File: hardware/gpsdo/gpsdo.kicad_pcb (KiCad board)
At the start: 2 copper layers, 6 parts, among them U1 74HC4040D_652, U2 74HC4040D_652

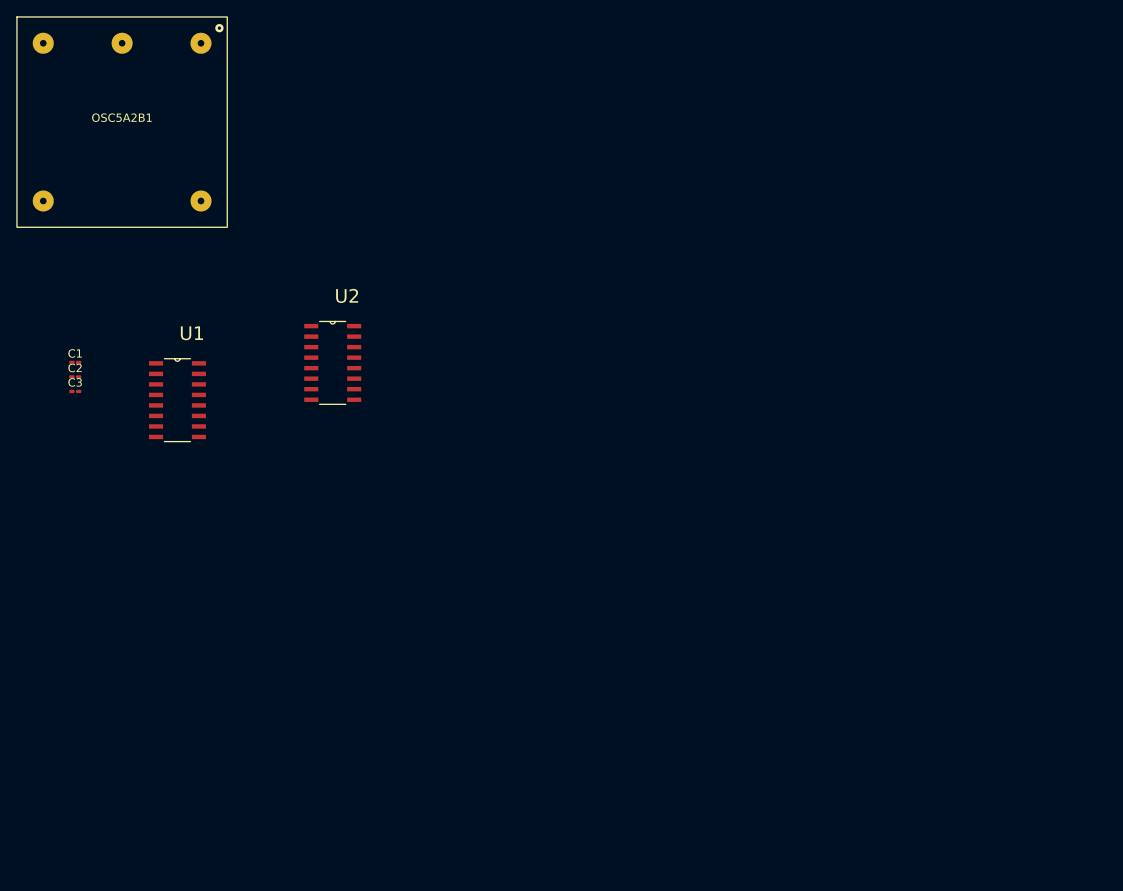
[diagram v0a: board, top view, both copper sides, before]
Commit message: update pcb; update hal
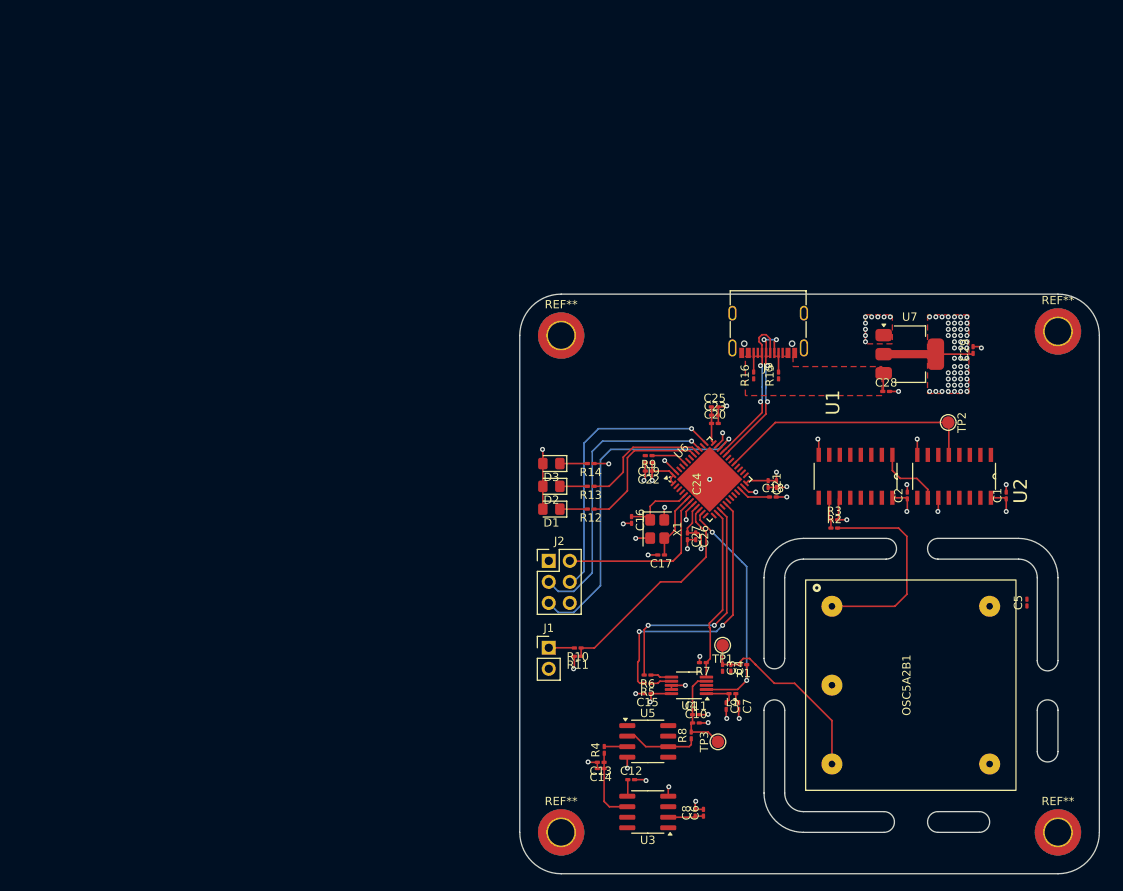
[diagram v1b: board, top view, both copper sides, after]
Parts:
- added C10: 10u, Capacitor_SMD:C_0201_0603Metric_Pad0.64x0.40mm_HandSolder, F.Cu at (129.0, 116.5)
- added C11: 100n, Capacitor_SMD:C_0201_0603Metric_Pad0.64x0.40mm_HandSolder, F.Cu at (129.0, 115.5)
- added C12: 1u, Capacitor_SMD:C_0201_0603Metric_Pad0.64x0.40mm_HandSolder, F.Cu at (121.2, 123.4)
- added C13: 10u, Capacitor_SMD:C_0201_0603Metric_Pad0.64x0.40mm_HandSolder, F.Cu at (117.5, 121.3)
- added C14: 100n, Capacitor_SMD:C_0201_0603Metric_Pad0.64x0.40mm_HandSolder, F.Cu at (117.5, 122.0)
- added C15: 100n, Capacitor_SMD:C_0201_0603Metric_Pad0.64x0.40mm_HandSolder, F.Cu at (123.2, 113.0)
- added C16: 12p, Capacitor_SMD:C_0201_0603Metric_Pad0.64x0.40mm_HandSolder, F.Cu at (121.2, 92.0)
- added C17: 12p, Capacitor_SMD:C_0201_0603Metric_Pad0.64x0.40mm_HandSolder, F.Cu at (124.8, 96.2)
- added C18: 4.7u, Capacitor_SMD:C_0201_0603Metric_Pad0.64x0.40mm_HandSolder, F.Cu at (138.3, 89.2)
- added C19: 100n, Capacitor_SMD:C_0201_0603Metric_Pad0.64x0.40mm_HandSolder, F.Cu at (123.3, 85.1)
- added C20: 100n, Capacitor_SMD:C_0201_0603Metric_Pad0.64x0.40mm_HandSolder, F.Cu at (131.3, 80.4)
- added C21: 100n, Capacitor_SMD:C_0201_0603Metric_Pad0.64x0.40mm_HandSolder, F.Cu at (137.8, 87.7)
- added C22: 100n, Capacitor_SMD:C_0201_0603Metric_Pad0.64x0.40mm_HandSolder, F.Cu at (123.3, 86.1)
- added C23: 100n, Capacitor_SMD:C_0201_0603Metric_Pad0.64x0.40mm_HandSolder, F.Cu at (131.3, 79.4)
- added C24: 100n, Capacitor_SMD:C_0201_0603Metric_Pad0.64x0.40mm_HandSolder, F.Cu at (138.8, 87.7)
- added C25: 4.7u, Capacitor_SMD:C_0201_0603Metric_Pad0.64x0.40mm_HandSolder, F.Cu at (131.3, 78.4)
- added C26: 1u, Capacitor_SMD:C_0201_0603Metric_Pad0.64x0.40mm_HandSolder, F.Cu at (129.0, 94.0)
- added C27: 100n, Capacitor_SMD:C_0201_0603Metric_Pad0.64x0.40mm_HandSolder, F.Cu at (128.0, 94.0)
- added C28: 10u, Capacitor_SMD:C_0201_0603Metric_Pad0.64x0.40mm_HandSolder, F.Cu at (152.0, 76.5)
- added C29: 10u, Capacitor_SMD:C_0201_0603Metric_Pad0.64x0.40mm_HandSolder, F.Cu at (162.5, 71.5)
- added C4: 100n, Capacitor_SMD:C_0201_0603Metric_Pad0.64x0.40mm_HandSolder, F.Cu at (133.2, 109.9)
- added C5: 100n, Capacitor_SMD:C_0201_0603Metric_Pad0.64x0.40mm_HandSolder, F.Cu at (169.0, 102.0)
- added C6: 1u, Capacitor_SMD:C_0201_0603Metric_Pad0.64x0.40mm_HandSolder, F.Cu at (129.9, 127.4)
- added C7: 100n, Capacitor_SMD:C_0201_0603Metric_Pad0.64x0.40mm_HandSolder, F.Cu at (134.2, 114.5)
- added C8: 100n, Capacitor_SMD:C_0201_0603Metric_Pad0.64x0.40mm_HandSolder, F.Cu at (128.9, 127.4)
- added C9: 100n, Capacitor_SMD:C_0201_0603Metric_Pad0.64x0.40mm_HandSolder, F.Cu at (132.7, 114.5)
- added D1: LED, LED_SMD:LED_0805_2012Metric_Pad1.15x1.40mm_HandSolder, F.Cu at (111.6, 90.7)
- added D2: LED, LED_SMD:LED_0805_2012Metric_Pad1.15x1.40mm_HandSolder, F.Cu at (111.6, 88.0)
- added D3: LED, LED_SMD:LED_0805_2012Metric_Pad1.15x1.40mm_HandSolder, F.Cu at (111.6, 85.2)
- added J1: Conn_01x02, Connector_PinHeader_2.54mm:PinHeader_1x02_P2.54mm_Vertical, F.Cu at (111.2, 107.5)
- added J2: Conn_02x03_Top_Bottom, Connector_PinHeader_2.54mm:PinHeader_2x03_P2.54mm_Vertical, F.Cu at (111.2, 97.0)
- added J3: USB_C_Receptacle_USB2.0_14P, Connector_USB:USB_C_Receptacle_G-Switch_GT-USB-7010ASV, F.Cu at (137.8, 68.1)
- added L1: 10u, Capacitor_SMD:C_0201_0603Metric_Pad0.64x0.40mm_HandSolder, F.Cu at (133.4, 113.0)
- added R1: 100, Resistor_SMD:R_0201_0603Metric_Pad0.64x0.40mm_HandSolder, F.Cu at (134.8, 109.5)
- added R10: 1.1k, Resistor_SMD:R_0201_0603Metric_Pad0.64x0.40mm_HandSolder, F.Cu at (114.8, 107.5)
- added R11: 2.2k, Resistor_SMD:R_0201_0603Metric_Pad0.64x0.40mm_HandSolder, F.Cu at (114.8, 108.5)
- added R12: 1.1k, Resistor_SMD:R_0201_0603Metric_Pad0.64x0.40mm_HandSolder, F.Cu at (116.3, 90.7)
- added R13: 1.1k, Resistor_SMD:R_0201_0603Metric_Pad0.64x0.40mm_HandSolder, F.Cu at (116.3, 88.0)
- added R14: 1.1k, Resistor_SMD:R_0201_0603Metric_Pad0.64x0.40mm_HandSolder, F.Cu at (116.3, 85.2)
- added R15: 22k, Resistor_SMD:R_0201_0603Metric_Pad0.64x0.40mm_HandSolder, F.Cu at (139.0, 74.6)
- added R16: 22k, Resistor_SMD:R_0201_0603Metric_Pad0.64x0.40mm_HandSolder, F.Cu at (136.0, 74.6)
- added R2: 1.1k, Resistor_SMD:R_0201_0603Metric_Pad0.64x0.40mm_HandSolder, F.Cu at (145.7, 93.0)
- added R3: 2.2k, Resistor_SMD:R_0201_0603Metric_Pad0.64x0.40mm_HandSolder, F.Cu at (145.7, 92.0)
- added R4: 33, Resistor_SMD:R_0201_0603Metric_Pad0.64x0.40mm_HandSolder, F.Cu at (118.0, 119.8)
- added R5: 100, Resistor_SMD:R_0201_0603Metric_Pad0.64x0.40mm_HandSolder, F.Cu at (123.2, 111.8)
- added R6: 100, Resistor_SMD:R_0201_0603Metric_Pad0.64x0.40mm_HandSolder, F.Cu at (123.2, 110.8)
- added R7: 10k, Resistor_SMD:R_0201_0603Metric_Pad0.64x0.40mm_HandSolder, F.Cu at (129.9, 109.2)
- added R8: 33, Resistor_SMD:R_0201_0603Metric_Pad0.64x0.40mm_HandSolder, F.Cu at (128.5, 118.0)
- added R9: 10k, Resistor_SMD:R_0201_0603Metric_Pad0.64x0.40mm_HandSolder, F.Cu at (123.3, 84.2)
- added REF**: MountingHole_3.2mm_M3_DIN965_Pad_TopBottom, MountingHole:MountingHole_3.2mm_M3_DIN965_Pad_TopBottom, F.Cu at (112.8, 69.8)
- added REF**: MountingHole_3.2mm_M3_DIN965_Pad_TopBottom, MountingHole:MountingHole_3.2mm_M3_DIN965_Pad_TopBottom, F.Cu at (172.8, 129.8)
- added REF**: MountingHole_3.2mm_M3_DIN965_Pad_TopBottom, MountingHole:MountingHole_3.2mm_M3_DIN965_Pad_TopBottom, F.Cu at (172.8, 69.2)
- added REF**: MountingHole_3.2mm_M3_DIN965_Pad_TopBottom, MountingHole:MountingHole_3.2mm_M3_DIN965_Pad_TopBottom, F.Cu at (112.8, 129.8)
- added TP1: TestPoint, TestPoint:TestPoint_Pad_D1.5mm, F.Cu at (132.2, 107.2)
- added TP2: TestPoint, TestPoint:TestPoint_Pad_D1.5mm, F.Cu at (159.5, 80.2)
- added TP3: TestPoint, TestPoint:TestPoint_Pad_D1.5mm, F.Cu at (131.7, 118.8)
- added U3: REF5040AD, Package_SO:SOIC-8_3.9x4.9mm_P1.27mm, F.Cu at (123.2, 127.3)
- added U4: AD5541A, Package_SO:MSOP-10_3x3mm_P0.5mm, F.Cu at (128.2, 112.0)
- added U5: OPA197xD, Package_SO:SOIC-8_3.9x4.9mm_P1.27mm, F.Cu at (123.2, 118.8)
- added U6: STM32F411CEUx, Package_DFN_QFN:QFN-48-1EP_7x7mm_P0.5mm_EP5.6x5.6mm, F.Cu at (130.7, 87.1)
- added U7: AMS1117-3.3, Package_TO_SOT_SMD:SOT-223-3_TabPin2, F.Cu at (154.8, 72.0)
- added X1: X322516MLB4SI, Crystal:Crystal_SMD_3225-4Pin_3.2x2.5mm, F.Cu at (124.3, 93.1)
- C3: value 100n -> 10u
- moved OSC5A2B1 117.0 mm to (155.0, 112.0), turned to 90 degrees
- moved C1 113.6 mm to (166.5, 89.1), turned to 90 degrees
- moved C2 101.5 mm to (154.6, 89.1), turned to 90 degrees
- moved C3 85.0 mm to (132.2, 109.9), turned to -90 degrees
- moved U1 82.4 mm to (148.3, 86.8), turned to -90 degrees
- moved U2 76.3 mm to (160.2, 86.8), turned to -90 degrees
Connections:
- C1 pad 1: VCC_5V -> VDDA_3V3
- C2 pad 1: VCC_5V -> VDDA_3V3
- C3 pad 1: VCC_5V -> Net-(OSC5A2B1-Vref)
- OSC5A2B1 pad 3: OCXO_Vref -> Net-(OSC5A2B1-Vref)
- U1 pad 10: OCXO_Out -> Net-(U1-~CP)
- U1 pad 16: VCC_5V -> VDDA_3V3
- U2 pad 16: VCC_5V -> VDDA_3V3
- U2 pad 5: OSCO_625KHZ -> OCXO_625KHZ
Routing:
- net GND: track 0.00 -> 56.7 mm, vias 0 -> 44
- net VDDA_3V3: track 0.00 -> 52.4 mm, vias 0 -> 58
- net SWDIO: track 0.00 -> 41.5 mm, vias 0 -> 1
- net SWO: track 0.00 -> 35.2 mm, vias 0 -> 1
- net SWCLK: track 0.00 -> 33.9 mm, vias 0 -> 1
- net AD5541A_DIN: track 0.00 -> 32.9 mm, vias 0 -> 2
- net OCXO_625KHZ: track 0.00 -> 31.9 mm
- net OCXO_Vref: track 0.00 -> 29.9 mm, vias 0 -> 2
- net AD5541A_SCLK: track 0.00 -> 29.1 mm, vias 0 -> 2
- net PPS_3V3: track 0.00 -> 27.1 mm
- net OCXO_Out: track 0.00 -> 25.5 mm
- net Net-(OSC5A2B1-Vref): track 0.00 -> 24.7 mm
- net AD5541A_CS: track 0.00 -> 21.1 mm
- net NRST: track 0.00 -> 20.7 mm
- net USB_P: track 0.00 -> 19.7 mm, vias 0 -> 2
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- added copper zone on F.Cu, net GND
- added copper zone on In1.Cu, net GND
- added copper zone on F.Cu, net VCC_5V
- added copper zone on F.Cu, net VDDA_3V3
- added copper zone on In2.Cu, net VDDA_3V3
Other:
- board outline added: 70 x 70 mm
- copper layers 2 -> 4

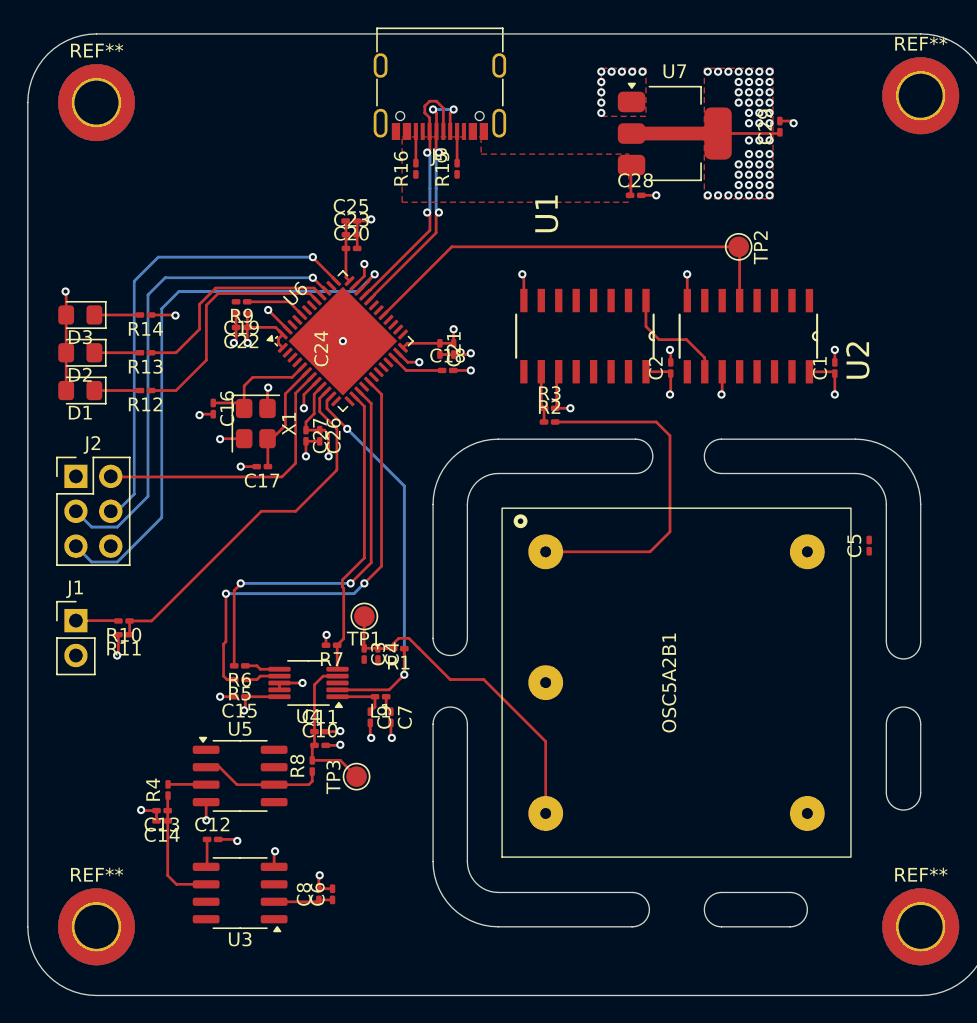
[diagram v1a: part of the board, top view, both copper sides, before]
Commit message: update hal; update schematics and routing
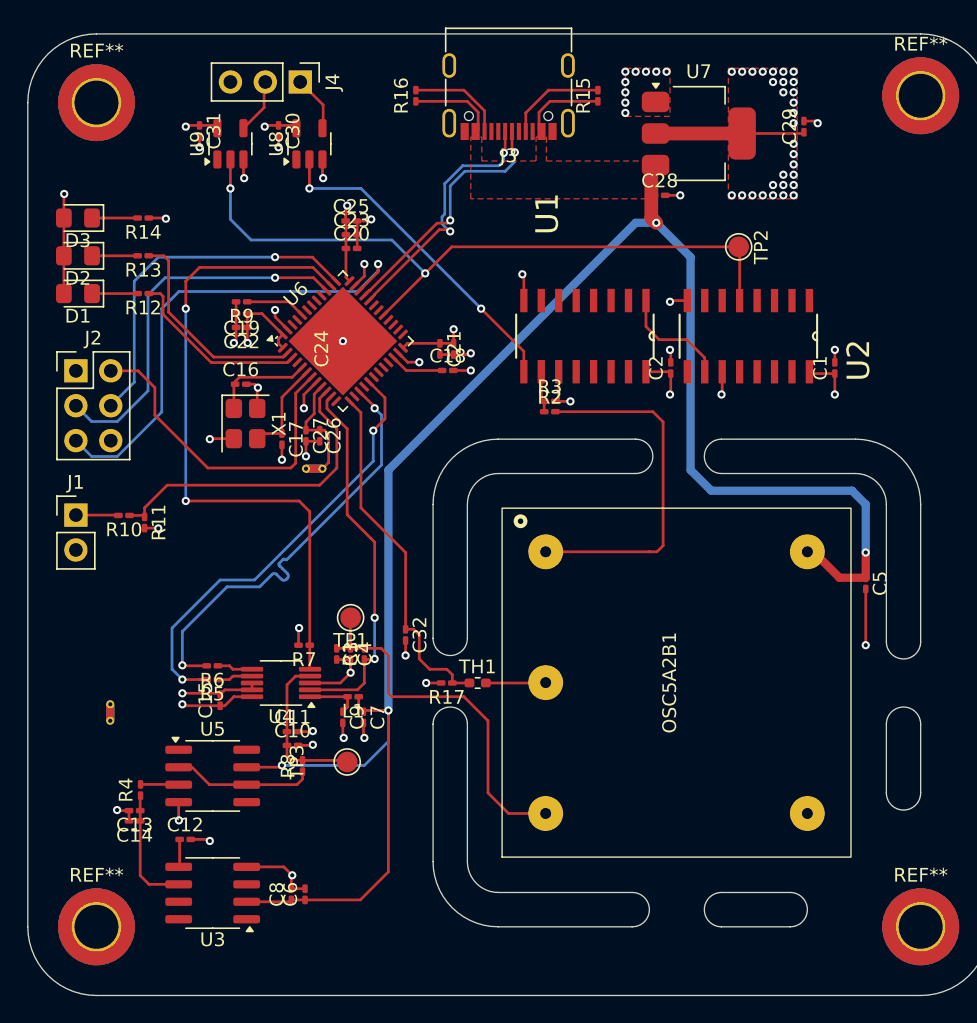
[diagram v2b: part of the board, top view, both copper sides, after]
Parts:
- added C30: 100n, Capacitor_SMD:C_0201_0603Metric_Pad0.64x0.40mm_HandSolder, F.Cu at (126.0, 71.8)
- added C31: 100n, Capacitor_SMD:C_0201_0603Metric_Pad0.64x0.40mm_HandSolder, F.Cu at (120.2, 71.8)
- added C32: 100n, Capacitor_SMD:C_0201_0603Metric_Pad0.64x0.40mm_HandSolder, F.Cu at (135.2, 108.5)
- added J4: Conn_01x03, Connector_PinHeader_2.54mm:PinHeader_1x03_P2.54mm_Vertical, F.Cu at (127.6, 68.2)
- added NT1: NetTie_2, NetTie:NetTie-2_THT_Pad0.3mm, F.Cu at (113.8, 114.8)
- added NT2: NetTie_2, NetTie:NetTie-2_THT_Pad0.3mm, F.Cu at (129.2, 96.4)
- added R17: 10k, Resistor_SMD:R_0201_0603Metric_Pad0.64x0.40mm_HandSolder, F.Cu at (138.2, 112.0)
- added TH1: NTCG103JF103FT1, Resistor_SMD:R_0402_1005Metric_Pad0.72x0.64mm_HandSolder, F.Cu at (140.5, 112.0)
- added U8: 74LVC1G17, Package_TO_SOT_SMD:SOT-23-5, F.Cu at (128.2, 72.8)
- added U9: 74LVC1G17, Package_TO_SOT_SMD:SOT-23-5, F.Cu at (122.5, 72.8)
- moved R15 11.5 mm to (149.2, 69.2)
- moved R11 8.30 mm to (116.2, 100.3), turned to -90 degrees
- moved R10 7.68 mm to (114.8, 99.8)
- moved J1 7.68 mm to (111.2, 99.8)
- moved J2 7.68 mm to (111.2, 89.3)
- moved D1 7.06 mm to (111.4, 83.7)
- moved D2 7.06 mm to (111.4, 80.9)
- moved D3 7.06 mm to (111.4, 78.2)
- moved R12 7.06 mm to (116.2, 83.7)
- moved R13 7.06 mm to (116.2, 80.9)
- moved R14 7.06 mm to (116.2, 78.2)
- moved R16 5.32 mm to (136.0, 69.2)
- moved J3 5.00 mm to (142.8, 68.1)
- moved C5 2.76 mm to (168.8, 104.8), turned to -90 degrees
- moved C16 2.67 mm to (123.2, 90.2), turned to 0 degrees
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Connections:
- C1 pad 1: VDDA_3V3 -> VDD_3V3
- C10 pad 2: GND -> GNDA
- C11 pad 2: GND -> GNDA
- C12 pad 2: GND -> GNDA
- C13 pad 2: GND -> GNDA
- C14 pad 2: GND -> GNDA
- C15 pad 1: VDDA_3V3 -> VDD_3V3
- C19 pad 1: VDDA_3V3 -> VDD_3V3
- C2 pad 1: VDDA_3V3 -> VDD_3V3
- C20 pad 1: VDDA_3V3 -> VDD_3V3
- C21 pad 1: VDDA_3V3 -> VDD_3V3
- C22 pad 1: VDDA_3V3 -> VDD_3V3
- C23 pad 1: VDDA_3V3 -> VDD_3V3
- C24 pad 1: VDDA_3V3 -> VDD_3V3
- C25 pad 1: VDDA_3V3 -> VDD_3V3
- C29 pad 1: VDDA_3V3 -> VDD_3V3
- C3 pad 2: GND -> GNDA
- C4 pad 2: GND -> GNDA
- C5 pad 2: GND -> GNDA
- C6 pad 2: GND -> GNDA
- C7 pad 2: GND -> GNDA
- C8 pad 2: GND -> GNDA
- C9 pad 2: GND -> GNDA
- D1 pad 2: VDDA_3V3 -> VDD_3V3
- D2 pad 2: VDDA_3V3 -> VDD_3V3
- D3 pad 2: VDDA_3V3 -> VDD_3V3
- J2 pad 1: VDDA_3V3 -> VDD_3V3
- OSC5A2B1 pad 2: GND -> GNDA
- R7 pad 2: VDDA_3V3 -> VDD_3V3
- U1 pad 16: VDDA_3V3 -> VDD_3V3
- U1 pad 9: unconnected-(U1-Q0-Pad9) -> OCXO_10MHZ
- U2 pad 16: VDDA_3V3 -> VDD_3V3
- U3 pad 4: GND -> GNDA
- U4 pad 10: VDDA_3V3 -> VDD_3V3
- U4 pad 3: GND -> GNDA
- U5 pad 4: GND -> GNDA
- U6 pad 1: VDDA_3V3 -> VDD_3V3
- U6 pad 13: unconnected-(U6-PA3-Pad13) -> OCXO_Temperature
- U6 pad 14: AD5541A_CS -> unconnected-(U6-PA4-Pad14)
- U6 pad 2: unconnected-(U6-PC13-Pad2) -> LED2
- U6 pad 24: VDDA_3V3 -> VDD_3V3
- U6 pad 3: unconnected-(U6-PC14-Pad3) -> LED1
- U6 pad 36: VDDA_3V3 -> VDD_3V3
- U6 pad 38: unconnected-(U6-PA15-Pad38) -> AD5541A_CS
- U6 pad 40: LED2 -> unconnected-(U6-PB4-Pad40)
- U6 pad 41: LED1 -> unconnected-(U6-PB5-Pad41)
- U6 pad 48: VDDA_3V3 -> VDD_3V3
- U7 pad 2: VDDA_3V3 -> VDD_3V3
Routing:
- net VCC_5V: track 7.79 -> 144.1 mm, vias 0 -> 4
- net VDD_3V3: track 0.00 -> 55.3 mm, vias 0 -> 41
- net VDDA_3V3: track 52.4 -> 8.10 mm, vias 58 -> 0
- net GNDA: track 0.00 -> 29.2 mm, vias 0 -> 11
- net AD5541A_CS: track 21.1 -> 48.5 mm, vias 0 -> 2
- net OCXO_Temperature: track 0.00 -> 25.9 mm
- net OCXO_10MHZ: track 0.00 -> 24.1 mm, vias 0 -> 2
- net OCXO_625KHZ: track 31.9 -> 52.0 mm, vias 0 -> 2
- net SWO: track 35.2 -> 27.5 mm
- net SWCLK: track 33.9 -> 26.4 mm
- net SWDIO: track 41.5 -> 35.5 mm
- net GND: track 56.7 -> 50.9 mm, vias 44 -> 37
- net Net-(J3-CC1): track 2.31 -> 7.29 mm
- net Net-(J3-CC2): track 2.31 -> 7.13 mm
- net Net-(J4-Pin_1): track 0.00 -> 4.07 mm
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- added copper zone on In1.Cu, net GNDA
- added copper zone on F.Cu, net VDD_3V3
- added copper zone on In2.Cu, net VDD_3V3
- removed copper zone on F.Cu, net VDDA_3V3
- removed copper zone on In2.Cu, net VDDA_3V3

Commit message: update routing
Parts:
- removed U8: 74LVC1G17, Package_TO_SOT_SMD:SOT-23-5
- added C33: 100n, Capacitor_SMD:C_0201_0603Metric_Pad0.64x0.40mm_HandSolder, F.Cu at (163.9, 73.8)
- added C34: 100n, Capacitor_SMD:C_0201_0603Metric_Pad0.64x0.40mm_HandSolder, F.Cu at (146.0, 73.8)
- added C35: 100n, Capacitor_SMD:C_0201_0603Metric_Pad0.64x0.40mm_HandSolder, F.Cu at (139.5, 73.8)
- added C36: 1u, Capacitor_SMD:C_0201_0603Metric_Pad0.64x0.40mm_HandSolder, F.Cu at (167.8, 82.2)
- added C37: 100n, Capacitor_SMD:C_0201_0603Metric_Pad0.64x0.40mm_HandSolder, F.Cu at (167.8, 83.0)
- added G***: LOGO, LOGO, F.Cu at (113.0, 109.0)
- added J5: Conn_Coaxial, Connector_Coaxial:SMA_Samtec_SMA-J-P-H-ST-EM1_EdgeMount, F.Cu at (174.8, 85.8)
- added NT3: NetTie_2, NetTie:NetTie-2_THT_Pad0.3mm, F.Cu at (170.6, 79.7)
- added R18: 33, Resistor_SMD:R_0201_0603Metric_Pad0.64x0.40mm_HandSolder, F.Cu at (170.5, 85.8)
- C30: value 100n -> 10u
- TP2: footprint TestPoint:TestPoint_Pad_D1.5mm -> TestPoint:TestPoint_Pad_D1.0mm
- U9: value 74LVC1G17 -> SN74LVC1G125DBV
- moved U9 46.6 mm to (167.2, 85.8), turned to 0 degrees
- moved C31 43.7 mm to (163.9, 73.0), turned to 0 degrees
- moved C30 37.9 mm to (163.9, 72.2), turned to 0 degrees
- moved TP2 13.2 mm to (170.8, 87.2), turned to 0 degrees
- moved R10 4.92 mm to (119.2, 97.8)
- moved R11 4.92 mm to (120.8, 98.3)
- moved C1 4.56 mm to (162.5, 91.2), turned to 180 degrees
- moved C2 1.71 mm to (152.8, 89.1)
- moved R2 1.71 mm to (144.0, 92.2)
- moved R3 1.71 mm to (144.0, 91.5)
- moved U1 1.71 mm to (146.6, 86.7)
- moved U2 1.71 mm to (158.5, 86.8)
- moved J1 1.30 mm to (111.2, 98.5)
- moved C28 0.75 mm to (153.8, 77.2)
- moved U7 0.75 mm to (156.6, 72.8)
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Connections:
- J4 pad 1: Net-(J4-Pin_1) -> OCXO_10MHZ
- J4 pad 2: Net-(J4-Pin_2) -> OCXO_625KHZ
- TP2 pad 1: OCXO_625KHZ -> Net-(J5-In)
- U9 pad 1: unconnected-(U9-NC-Pad1) -> OCXO_Out
- U9 pad 2: OCXO_625KHZ -> OCXO_Out
- U9 pad 3: GND -> GNDA
- U9 pad 4: Net-(J4-Pin_2) -> Net-(R18-Pad2)
- U9 pad 5: VDD_3V3 -> VCC_5V
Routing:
- net OCXO_Out: track 25.9 -> 46.9 mm
- net VCC_5V: track 144.1 -> 159.5 mm, vias 4 -> 5
- net VDD_3V3: track 55.3 -> 45.4 mm, vias 41 -> 32
- net GNDA: track 29.2 -> 38.3 mm, vias 11 -> 15
- net USB_P: track 18.8 -> 25.7 mm
- net Net-(J5-In): track 0.00 -> 5.50 mm
- net PPS_3V3: track 23.3 -> 18.0 mm
- net GND: track 50.9 -> 56.1 mm, vias 37 -> 38
- net USB_N: track 19.2 -> 24.2 mm
- net AD5541A_CS: track 48.5 -> 43.7 mm
- net PPS_5V: track 3.10 -> 7.91 mm
- net Net-(J4-Pin_1): track 4.07 -> 0.00 mm
- net Net-(J4-Pin_2): track 4.02 -> 0.00 mm
- net OCXO_10MHZ: track 24.1 -> 27.1 mm
- net Net-(R18-Pad2): track 0.00 -> 2.44 mm
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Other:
- board text added: "10MHz"
- board text added: "625kHz"
- board text added: "GPSDO v1"
- board text added: "NRST 3V3 SWCLK SWO GND SWDIO"
- board text added: "PPS"
- board text added: "VDAC"
- board text added: "VOSC"
